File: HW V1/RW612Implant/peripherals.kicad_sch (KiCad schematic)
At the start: 0 parts

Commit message: clocked up on a saturday
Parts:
- added C7: 2.2u, Capacitor_SMD:C_0201_0603Metric, symbol Device:C
- added R2: 400R, Resistor_SMD:R_0201_0603Metric, symbol Device:R
- added R3: 166R, Resistor_SMD:R_0201_0603Metric, symbol Device:R
- added R4: 133R, Resistor_SMD:R_0201_0603Metric, symbol Device:R
- added U4: IM67D128BV01, Library:PG-TLGA-5-8, symbol New_Library:IM67D128BV01
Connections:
- net MIC_C: now also U4.4 (CLK)
- net MIC_D: now also U4.1 (DATA)
- new net +1V8: C7.1, U4.5 (VDD)
- new net GND: C7.2, U4.2 (LR), U4.3 (GND)
- new net LED_B: R4.1
- new net LED_G: R3.1
- new net LED_R: R2.1
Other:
- note added: "VIO1 = 1V8"
- note removed: "IM67D128BV01 microphone"

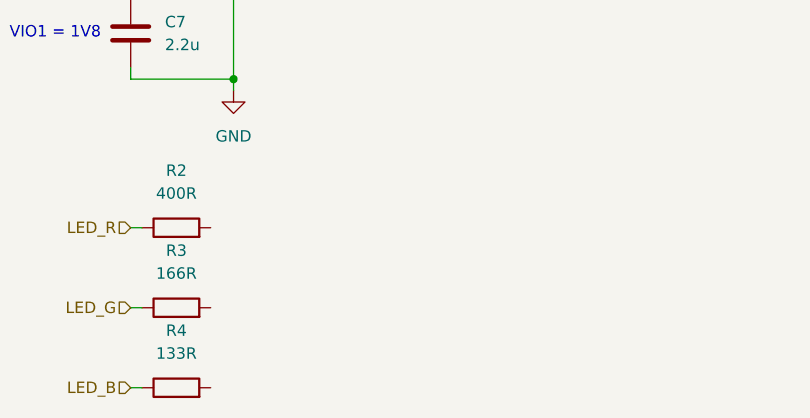
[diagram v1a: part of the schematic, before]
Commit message: we do a little led routing
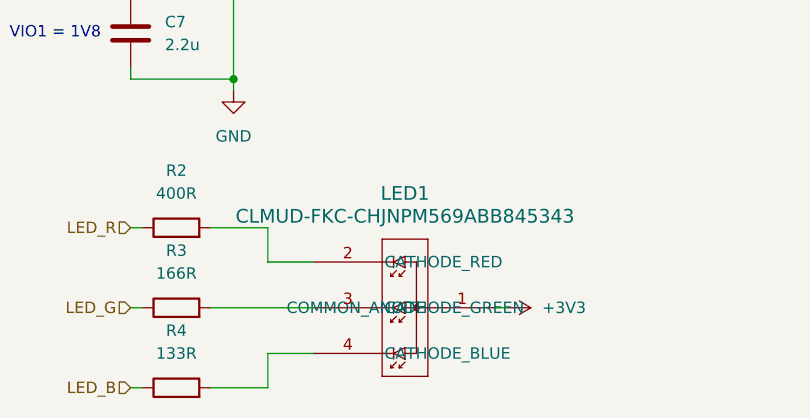
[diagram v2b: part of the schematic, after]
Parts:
- added LED1: CLMUD-FKC-CHJNPM569ABB845343, Library:PLCC4_CLMUD-FKC_CRW, symbol New_Library:CLMUD-FKC-CHJNPM569ABB845343
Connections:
- net at R2.2: now also LED1.2 (CATHODE_RED)
- net at R4.2: now also LED1.4 (CATHODE_BLUE)
- net at R3.2: now also LED1.3 (CATHODE_GREEN)
- new net +3V3: LED1.1 (COMMON_ANODE)
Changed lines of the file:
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@@
+	(wire
+		(pts
+			(xy 82.55 110.49) (xy 82.55 114.3)
+		)
+		(stroke
+			(width 0)
+			(type default)
+		)
+	)
 	(wire
 		(pts
@@
 	(wire
 		(pts
+			(xy 87.63 110.49) (xy 82.55 110.49)
+		)
+		(stroke
+			(width 0)
+			(type default)
+		)
+	)
+	(wire
+		(pts
 			(xy 66.04 59.69) (xy 67.31 59.69)
 		)
@@
 	(wire
 		(pts
+			(xy 87.63 100.33) (xy 82.55 100.33)
+		)
+		(stroke
+			(width 0)
+			(type default)
+		)
+	)
+	(wire
+		(pts
+			(xy 82.55 114.3) (xy 76.2 114.3)
+		)
+		(stroke
+			(width 0)
+			(type default)
+		)
+	)
+	(wire
+		(pts
 			(xy 67.31 105.41) (xy 68.58 105.41)
 		)
@@
 	(wire
 		(pts
+			(xy 76.2 105.41) (xy 87.63 105.41)
+		)
+		(stroke
+			(width 0)
+			(type default)
+		)
+	)
+	(wire
+		(pts
 			(xy 66.04 64.77) (xy 67.31 64.77)
 		)
@@
 	(wire
 		(pts
+			(xy 82.55 96.52) (xy 76.2 96.52)
+		)
+		(stroke
+			(width 0)
+			(type default)
+		)
+	)
+	(wire
+		(pts
+			(xy 82.55 100.33) (xy 82.55 96.52)
+		)
+		(stroke
+			(width 0)
+			(type default)
+		)
+	)
+	(wire
+		(pts
 			(xy 67.31 69.85) (xy 67.31 71.12)
+		)
+		(stroke
+			(width 0)
+			(type default)
+		)
+	)
+	(wire
+		(pts
+			(xy 107.95 105.41) (xy 109.22 105.41)
 		)
 		(stroke
@@
 	)
 	(symbol
+		(lib_id "New_Library:CLMUD-FKC-CHJNPM569ABB845343")
+		(at 107.95 105.41 180)
+		(unit 1)
+		(exclude_from_sim no)
+		(in_bom yes)
+		(on_board yes)
+		(dnp no)
+		(fields_autoplaced yes)
+		(property "Reference" "LED1"
+			(at 97.79 92.71 0)
+			(effects
+				(font
+					(size 1.524 1.524)
+				)
+			)
+		)
+		(property "Value" "CLMUD-FKC-CHJNPM569ABB845343"
+			(at 97.79 95.25 0)
+			(effects
+				(font
+					(size 1.524 1.524)
+				)
+			)
+		)
+		(property "Footprint" "Library:PLCC4_CLMUD-FKC_CRW"
+			(at 107.95 105.41 0)
+			(effects
+				(font
+					(size 1.27 1.27)
+					(italic yes)
+				)
+				(hide yes)
+			)
+		)
+		(property "Datasheet" "CLMUD-FKC-CHJNPM569ABB845343"
+			(at 107.95 105.41 0)
+			(effects
+				(font
+					(size 1.27 1.27)
+					(italic yes)
+				)
+				(hide yes)
+			)
+		)
+		(property "Description" ""
+			(at 107.95 105.41 0)
+			(effects
+				(font
+					(size 1.27 1.27)
+				)
+				(hide yes)
+			)
+		)
+		(pin "3"
+		)
+		(pin "4"
+		)
+		(pin "1"
+		)
+		(pin "2"
+		)
+		(instances
+			(project ""
+				(path "/a22e6eb7-bd70-4e22-bc03-a0cb284c787e/9311bce5-b6b9-499c-b401-cf55b3154c79"
+					(reference "LED1")
+					(unit 1)
+				)
+			)
+		)
+	)
+	(symbol
 		(lib_id "Device:C")
 		(at 67.31 74.93 0)
@@
 					(unit 1)
 				)
+			)
+		)
+	)
+	(symbol
+		(lib_id "power:+3V3")
+		(at 109.22 105.41 270)
+		(unit 1)
+		(exclude_from_sim no)
+		(in_bom yes)
+		(on_board yes)
+		(dnp no)
+		(fields_autoplaced yes)
+		(property "Reference" "#PWR037"
+			(at 105.41 105.41 0)
+			(effects
+				(font
+					(size 1.27 1.27)
+				)
+				(hide yes)
+			)
+		)
+		(property "Value" "+3V3"
+			(at 113.03 105.4099 90)
+			(effects
+				(font
+					(size 1.27 1.27)
+				)
+				(justify left)
+			)
+		)
+		(property "Footprint" ""
+			(at 109.22 105.41 0)
+			(effects
+				(font
+					(size 1.27 1.27)
+				)
+				(hide yes)
+			)
+		)
+		(property "Datasheet" ""
+			(at 109.22 105.41 0)
+			(effects
+				(font
+					(size 1.27 1.27)
+				)
+				(hide yes)
+			)
+		)
+		(property "Description" "Power symbol creates a global label with name \"+3V3\""
+			(at 109.22 105.41 0)
+			(effects
+				(font
+					(size 1.27 1.27)
+				)
+				(hide yes)
+			)
+		)
+		(pin "1"
+		)
+		(instances
+			(project ""
+				(path "/a22e6eb7-bd70-4e22-bc03-a0cb284c787e/9311bce5-b6b9-499c-b401-cf55b3154c79"
+					(reference "#PWR037")
+					(unit 1)
+				)

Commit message: everything except temp and qi?
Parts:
- added IC3: NMH1000T1, Library:NMH1000T1, symbol New_Library:NMH1000T1
- LED1: value CLMUD-FKC-CHJNPM569ABB845343 -> CLMUD-FKC
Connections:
- net +1V8: now also IC3.1 (VDD), IC3.3 (ODR-SCL)
- net GND: now also IC3.2 (TH-SDA), IC3.4 (VSS), IC3.5 (MODE)
- new net B_SWITCH: IC3.6 (OUT)
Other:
- note added: "STTS22H temperature sensor - 3.3v"
- note removed: "CLMUD-FKC LED"
- note removed: "NMH1000 magnetic switch - high sample rate"

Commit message: gods greatest decoupler
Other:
- note added: "LSM6DSV16B IMU/TEMP"
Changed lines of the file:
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@@
+		)
+	)
+	(text "LSM6DSV16B IMU/TEMP"
+		(exclude_from_sim no)
+		(at 135.382 93.98 0)
+		(effects
+			(font
+				(size 1.27 1.27)
+			)
 		)
 	)
